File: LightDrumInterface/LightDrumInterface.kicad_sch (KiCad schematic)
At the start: 81 parts, among them J1 MIDI-IN, J2 0525593652, J2 Micro_SD_Card, J4 PWR-CONN, J5 MIDI-OUT, J6 0541323662, Q1 NX6008NBKWX, Q2 NX6008NBKWX, Q3 NX6008NBKWX, Q4 NX6008NBKWX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

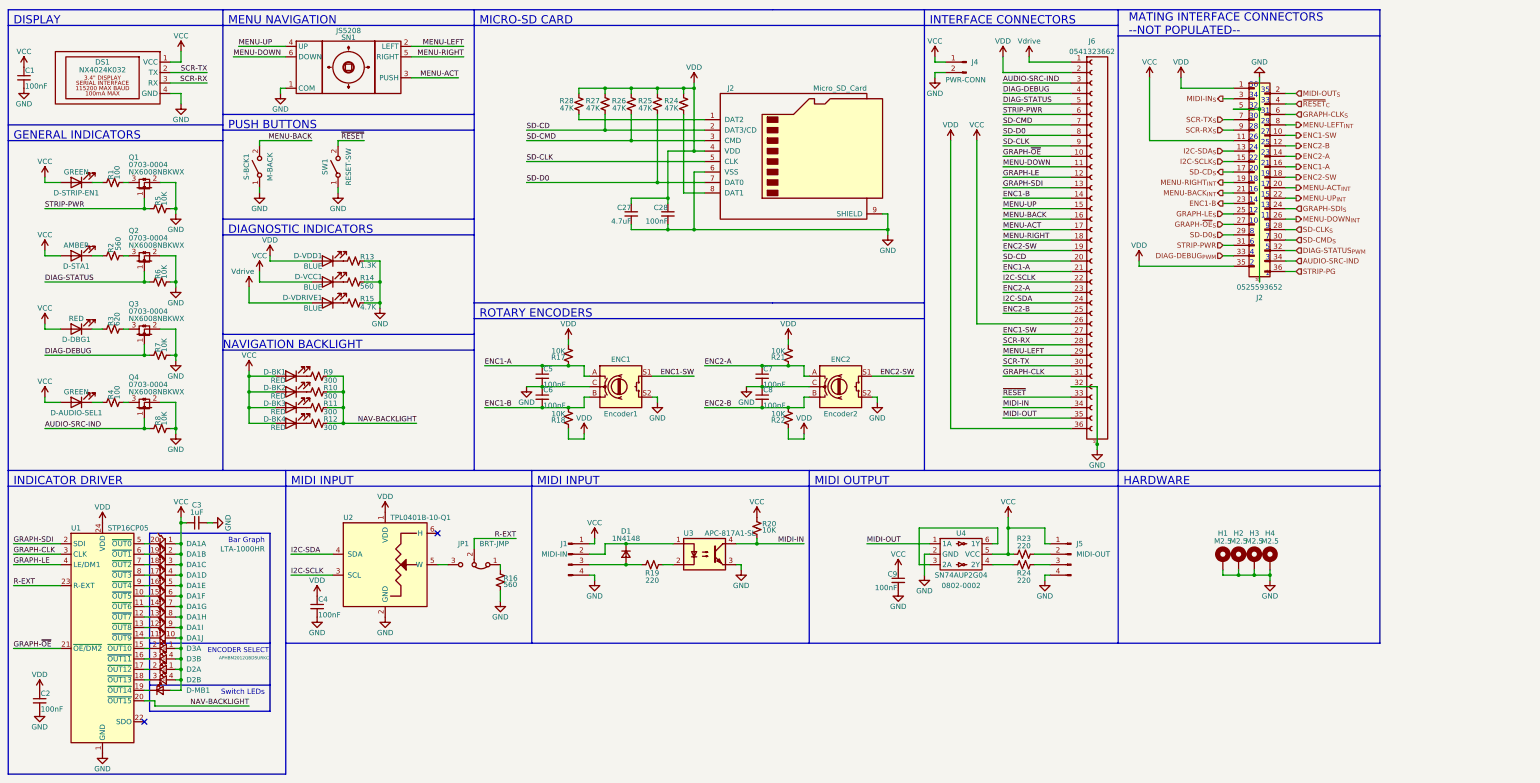
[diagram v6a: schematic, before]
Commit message: add screen control and more display layout
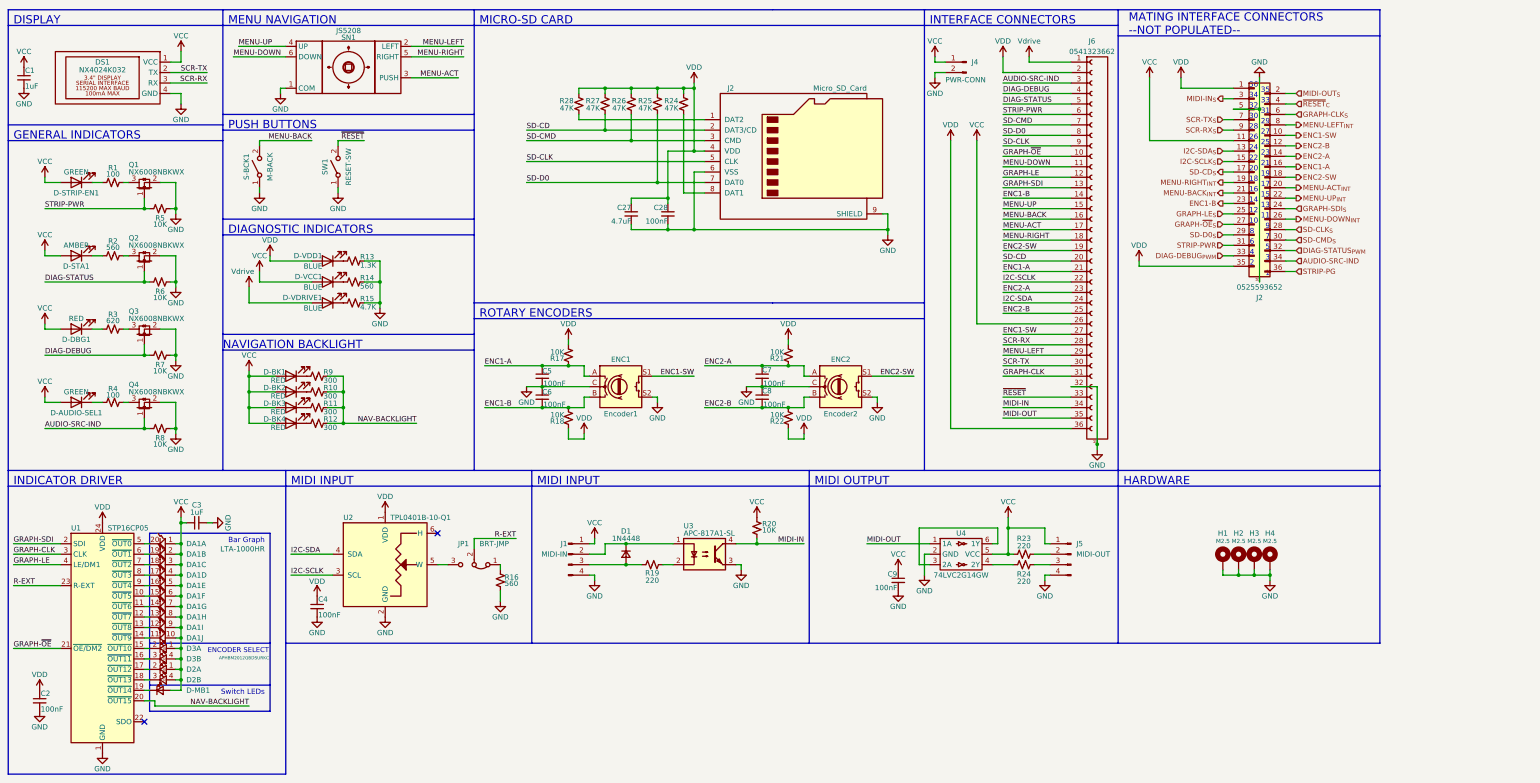
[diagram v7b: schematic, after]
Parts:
- C1: value 100nF -> 1uF; footprint Capacitor_SMD:C_0402_1005Metric -> Capacitor_SMD:C_0603_1608Metric
- D1: value 1N4148 -> 1N4448; SupplierPN 1N4148WS-FDICT-ND -> 1N4448WSQ-7-FDICT-ND
- U4: value SN74AUP2G04 -> 74LVC2G14GW; PartNumber 0802-0002 -> (none); SupplierPN 296-27353-1-ND -> 1727-4217-1-ND
